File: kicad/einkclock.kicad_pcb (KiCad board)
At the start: 2 copper layers, 80 x 100 mm, 66 parts, among them P1 SWD, Q1 IRLIB9343PBF, Q2 IRLIB9343PBF, Q3 IRLU120N, Q4 IRLU120N, U1 MCP1702-3302ETO, U2 MC33063A, U3 MC33063A, U4 MC78L15ACP, U5 MC79L15ACP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

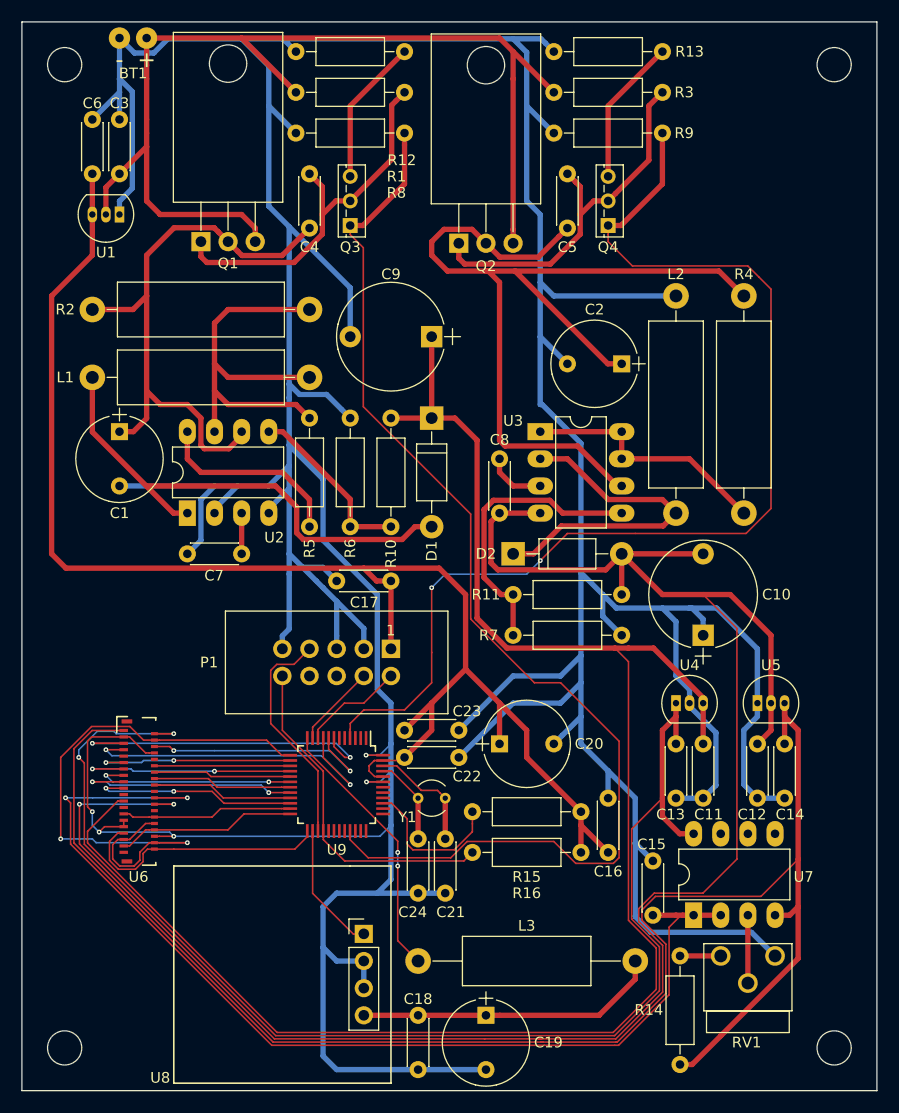
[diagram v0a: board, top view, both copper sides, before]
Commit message: Add ground layer
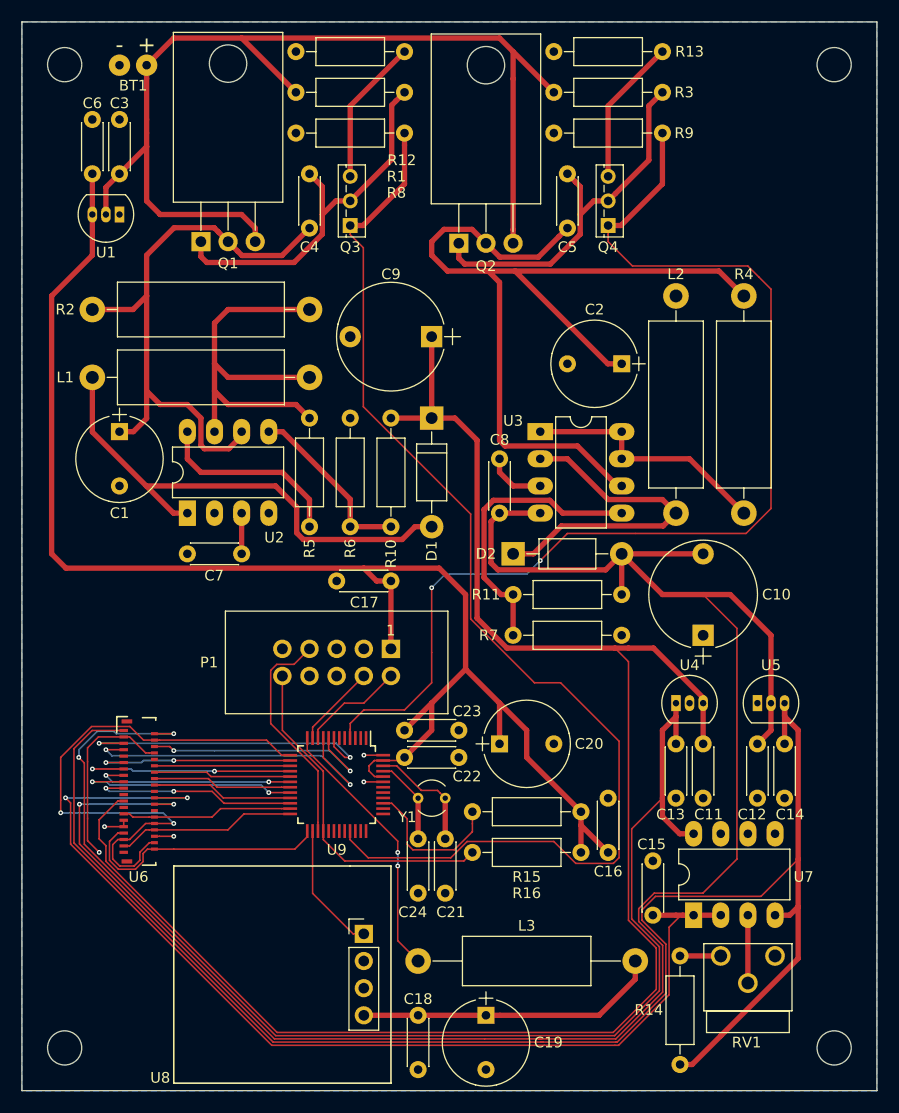
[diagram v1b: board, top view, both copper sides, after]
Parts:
- moved BT1 2.54 mm to (24.1, 19.1)
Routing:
- net GND: track 581.4 -> 25.4 mm
- net /DON: track 58.1 -> 53.4 mm
- net +BATT: track 101.3 -> 99.8 mm
- net /DCL: track 30.4 -> 29.1 mm
- net /+22V: track 163.7 -> 162.8 mm
- added copper zone on B.Cu, net GND
